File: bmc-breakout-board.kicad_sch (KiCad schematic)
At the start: 7 parts

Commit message: [#92504] Prepare schematic for new peripherals
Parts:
- removed TP1, TP2: 5001, bmc-breakout-board-footprints:Test_Point_D1.02mm, symbol bmc-breakout-board:5001
- N1: footprint bmc-breakout-board-footprints:antmicro-logo_scaled_20mm_mask -> antmicro-footprints:antmicro-logo_scaled_20mm_mask
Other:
- removed sheet Edge Connectors
- added sheet DC-SCM 2.1 connector (dc-scm-connector.kicad_sch)
- moved on the sheet: N1, N2

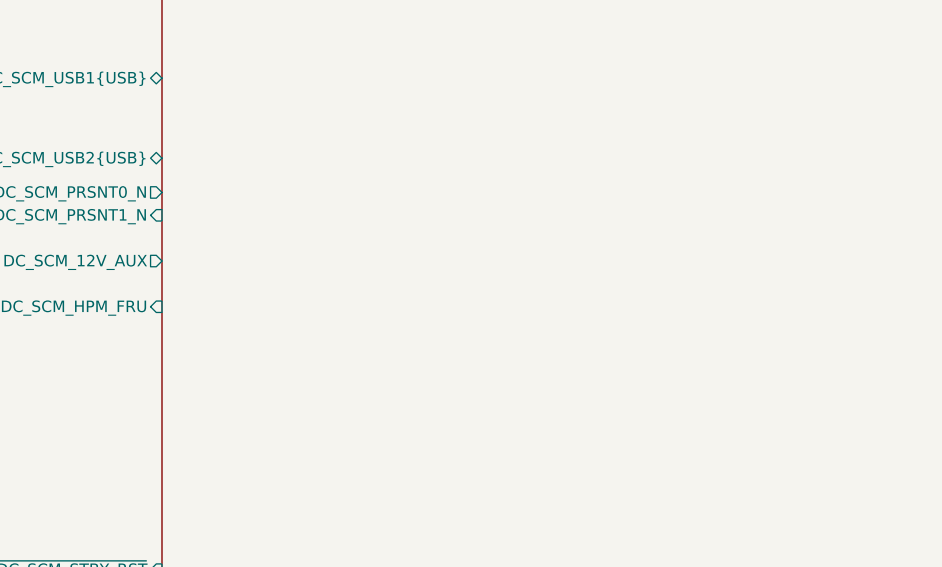
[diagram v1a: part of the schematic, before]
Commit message: [#92504] Create power schematic, change 12V connector
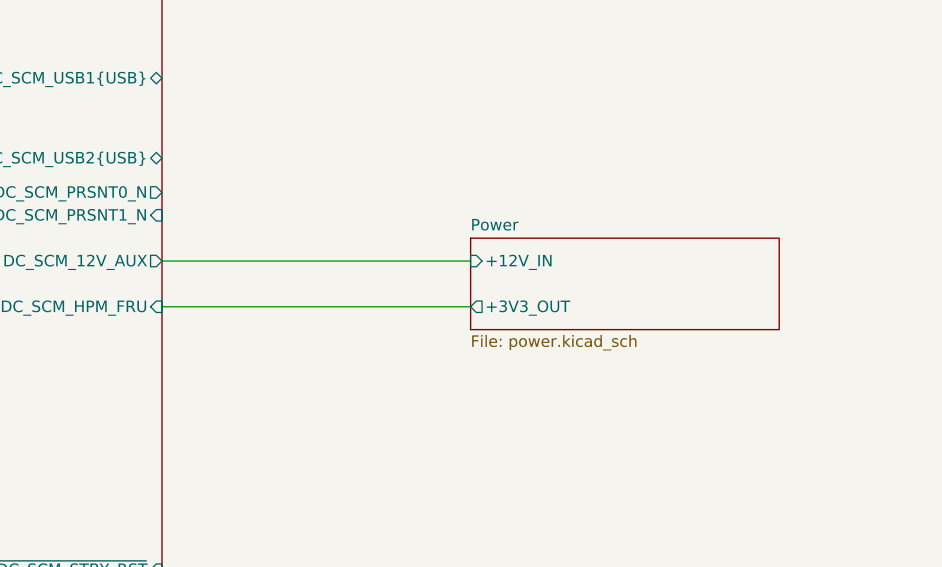
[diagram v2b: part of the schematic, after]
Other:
- added sheet Power (power.kicad_sch)
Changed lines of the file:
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@@
+		)
+	)
+	(wire
+		(pts
+			(xy 57.15 59.69) (xy 91.44 59.69)
+		)
+		(stroke
+			(width 0)
+			(type default)
+		)
+	)
+	(wire
+		(pts
+			(xy 57.15 64.77) (xy 91.44 64.77)
+		)
+		(stroke
+			(width 0)
+			(type default)
 		)
 	)
@@
 				)
 			)
+		)
+	)
+	(sheet
+		(at 91.44 57.15)
+		(size 34.29 10.16)
+		(exclude_from_sim no)
+		(in_bom yes)
+		(on_board yes)
+		(dnp no)
+		(fields_autoplaced yes)
+		(stroke
+			(width 0.1524)
+			(type solid)
+		)
+		(fill
+			(color 0 0 0 0.0000)
+		)
+		(property "Sheetname" "Power"
+			(at 91.44 56.4384 0)
+			(effects
+				(font
+					(size 1.27 1.27)
+				)
+				(justify left bottom)
+			)
+		)
+		(property "Sheetfile" "power.kicad_sch"
+			(at 91.44 67.8946 0)
+			(effects
+				(font
+					(size 1.27 1.27)
+				)
+				(justify left top)
+			)
+		)
+		(pin "+12V_IN" input
+			(at 91.44 59.69 180)
+			(effects
+				(font
+					(size 1.27 1.27)
+				)
+				(justify left)
+			)
+		)
+		(pin "+3V3_OUT" output
+			(at 91.44 64.77 180)
+			(effects
+				(font
+					(size 1.27 1.27)
+				)
+				(justify left)
+			)
+		)
+		(instances
+			(project "bmc-breakout-board"
+				(path "/5d67ef28-5805-4f87-b722-2926dabf7f6e"
+					(page "3")
+				)
+			)

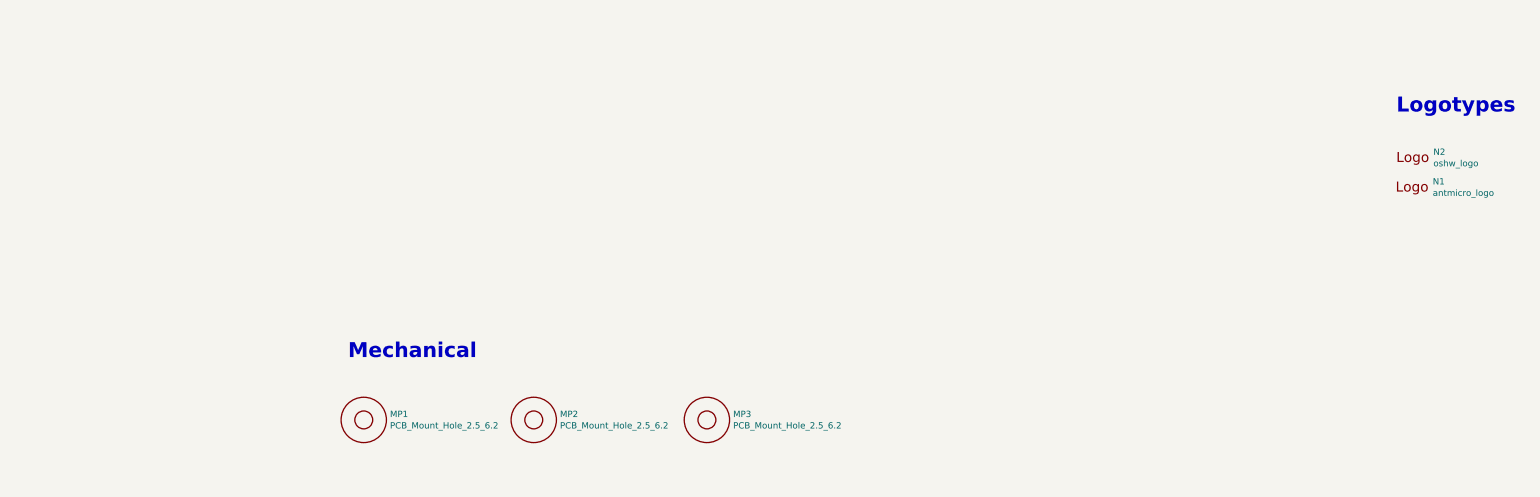
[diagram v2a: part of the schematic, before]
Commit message: [#92504] Remove micro USB and USB A
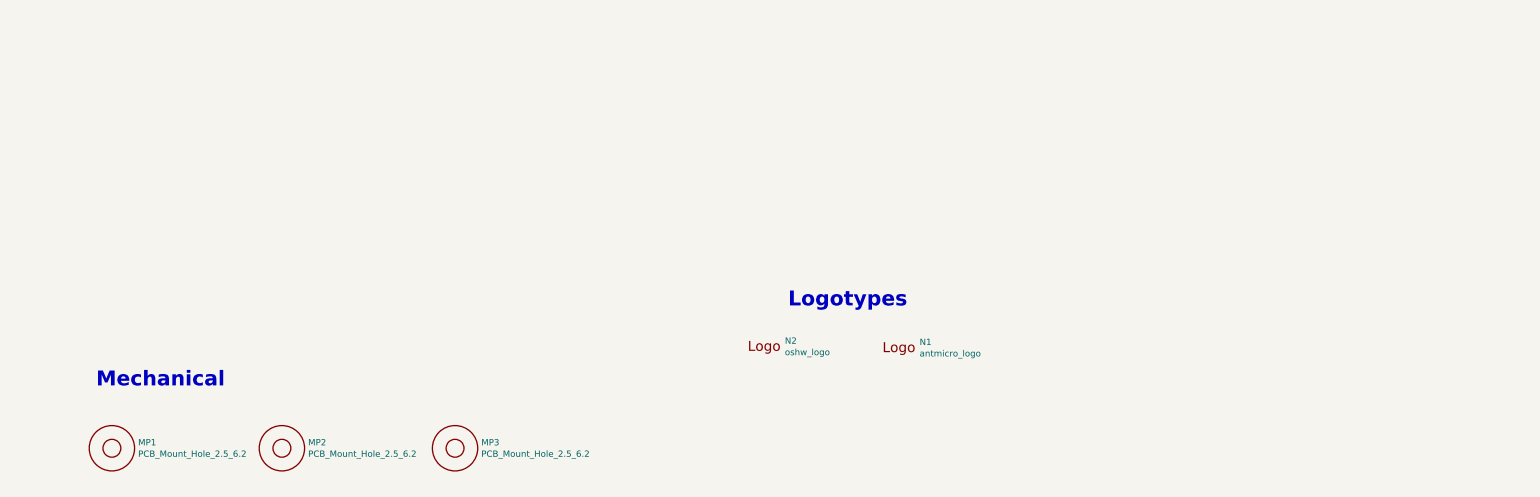
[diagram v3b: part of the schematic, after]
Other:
- moved on the sheet: MP1, MP2, MP3, N1, N2
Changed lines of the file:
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@@
 	(text "Logotypes"
 		(exclude_from_sim no)
-		(at 378.46 208.28 0)
+		(at 255.778 247.396 0)
 		(effects
 			(font
@@
 	(text "Mechanical"
 		(exclude_from_sim no)
-		(at 167.005 257.81 0)
+		(at 116.205 263.525 0)
 		(effects
 			(font
@@
 	)
 	(image
-		(at 392.43 240.03)
+		(at 288.925 272.415)
 		(scale 0.15)
 		(data "iVBORw0KGgoAAAANSUhEUgAABLAAAASwCAIAAABkQySYAAAAA3NCSVQICAjb4U/gAAAACXBIWXMA"
@@
 	)
 	(image
-		(at 354.33 239.8522)
+		(at 250.825 272.2372)
 		(scale 0.4)
 		(data "iVBORw0KGgoAAAANSUhEUgAABPcAAAGUCAYAAABZQseRAAAABHNCSVQICAgIfAhkiAAAAAlwSFlz"
@@
 	(symbol
 		(lib_id "bmc-breakout-board:antmicro_logo")
-		(at 380.365 224.155 0)
+		(at 276.86 256.54 0)
 		(unit 1)
 		(exclude_from_sim no)
@@
 		(dnp no)
 		(property "Reference" "N1"
-			(at 385.8006 221.7928 0)
+			(at 282.2956 254.1778 0)
 			(effects
 				(font
@@
 		)
 		(property "Value" "antmicro_logo"
-			(at 385.8006 224.1042 0)
+			(at 282.2956 256.4892 0)
 			(effects
 				(font
@@
 		)
 		(property "Footprint" "antmicro-footprints:antmicro-logo_scaled_20mm_mask"
-			(at 377.825 217.805 0)
+			(at 274.32 250.19 0)
 			(effects
 				(font
@@
 		)
 		(property "Datasheet" ""
-			(at 380.365 215.265 0)
+			(at 276.86 247.65 0)
 			(effects
 				(font
@@
 		)
 		(property "Description" ""
-			(at 380.365 224.155 0)
+			(at 276.86 256.54 0)
 			(effects
 				(font
@@
 	(symbol
 		(lib_id "bmc-breakout-board:oshw_logo")
-		(at 381 215.9 0)
+		(at 250.19 254 0)
 		(unit 1)
 		(exclude_from_sim no)
@@
 		(dnp no)
 		(property "Reference" "N2"
-			(at 385.9276 215.8238 0)
+			(at 255.1176 253.9238 0)
 			(effects
 				(font
@@
 		)
 		(property "Value" "oshw_logo"
-			(at 385.9276 218.1352 0)
+			(at 255.1176 256.2352 0)
 			(effects
 				(font
@@
 		)
 		(property "Footprint" "bmc-breakout-board-footprints:oshw-logo"
-			(at 381.508 221.996 0)
+			(at 250.698 260.096 0)
 			(effects
 				(font
@@
 		)
 		(property "Datasheet" ""
-			(at 381 215.9 0)
+			(at 250.19 254 0)
 			(effects
 				(font
@@
 		)
 		(property "Description" ""
-			(at 381 215.9 0)
+			(at 250.19 254 0)
 			(effects
 				(font
@@
 	(symbol
 		(lib_id "bmc-breakout-board:PCB_Mount_Hole_2.5_6.2")
-		(at 204.47 269.875 0)
+		(at 153.67 275.59 0)
 		(unit 1)
 		(exclude_from_sim no)
@@
 		(dnp no)
 		(property "Reference" "MP2"
-			(at 209.7532 268.7066 0)
+			(at 158.9532 274.4216 0)
 			(effects
 				(font
@@
 		)
 		(property "Value" "PCB_Mount_Hole_2.5_6.2"
-			(at 209.7532 271.018 0)
+			(at 158.9532 276.733 0)
 			(effects
 				(font
@@
 		)
 		(property "Footprint" "bmc-breakout-board-footprints:Mount-hole-M2.5"
-			(at 224.79 252.095 0)
+			(at 173.99 257.81 0)
 			(effects
 				(font
@@
 		)
 		(property "Datasheet" ""
-			(at 228.6 249.555 0)
+			(at 177.8 255.27 0)
 			(effects
 				(font
@@
 		)
 		(property "Description" ""
-			(at 204.47 269.875 0)
+			(at 153.67 275.59 0)
 			(effects
 				(font
@@
 	(symbol
 		(lib_id "bmc-breakout-board:PCB_Mount_Hole_2.5_6.2")
-		(at 239.395 269.875 0)
+		(at 188.595 275.59 0)
 		(unit 1)
 		(exclude_from_sim no)
@@
 		(dnp no)
 		(property "Reference" "MP3"
-			(at 244.6782 268.7066 0)
+			(at 193.8782 274.4216 0)
 			(effects
 				(font
@@
 		)
 		(property "Value" "PCB_Mount_Hole_2.5_6.2"
-			(at 244.6782 271.018 0)
+			(at 193.8782 276.733 0)
 			(effects
 				(font
@@
 		)
 		(property "Footprint" "bmc-breakout-board-footprints:Mount-hole-M2.5"
-			(at 259.715 252.095 0)
+			(at 208.915 257.81 0)
 			(effects
 				(font
@@
 		)
 		(property "Datasheet" ""
-			(at 263.525 249.555 0)
+			(at 212.725 255.27 0)
 			(effects
 				(font
@@
 		)
 		(property "Description" ""
-			(at 239.395 269.875 0)
+			(at 188.595 275.59 0)
 			(effects
 				(font
@@
 	(symbol
 		(lib_id "bmc-breakout-board:PCB_Mount_Hole_2.5_6.2")
-		(at 170.18 269.875 0)
+		(at 119.38 275.59 0)
 		(unit 1)
 		(exclude_from_sim no)
@@
 		(dnp no)
 		(property "Reference" "MP1"
-			(at 175.4632 268.7066 0)
+			(at 124.6632 274.4216 0)
 			(effects
 				(font
@@
 		)
 		(property "Value" "PCB_Mount_Hole_2.5_6.2"
-			(at 175.4632 271.018 0)
+			(at 124.6632 276.733 0)
 			(effects
 				(font
@@
 		)
 		(property "Footprint" "bmc-breakout-board-footprints:Mount-hole-M2.5"
-			(at 190.5 252.095 0)
+			(at 139.7 257.81 0)
 			(effects
 				(font
@@
 		)
 		(property "Datasheet" ""
-			(at 194.31 249.555 0)
+			(at 143.51 255.27 0)
 			(effects
 				(font
@@
 		)
 		(property "Description" ""
-			(at 170.18 269.875 0)
+			(at 119.38 275.59 0)
 			(effects
 				(font

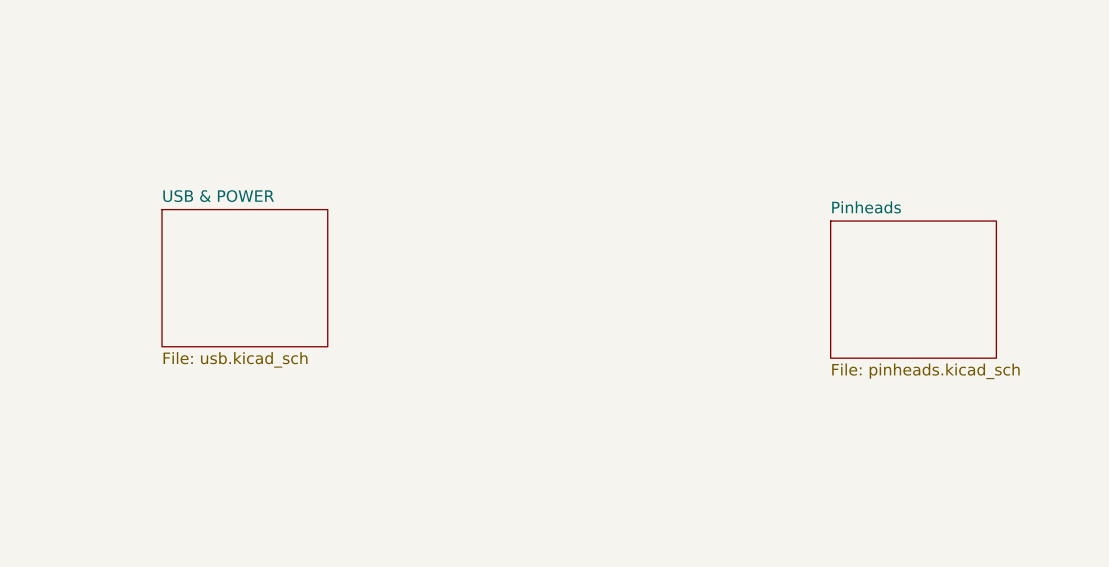
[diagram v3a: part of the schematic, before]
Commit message: [#92504] Remove old pinheads
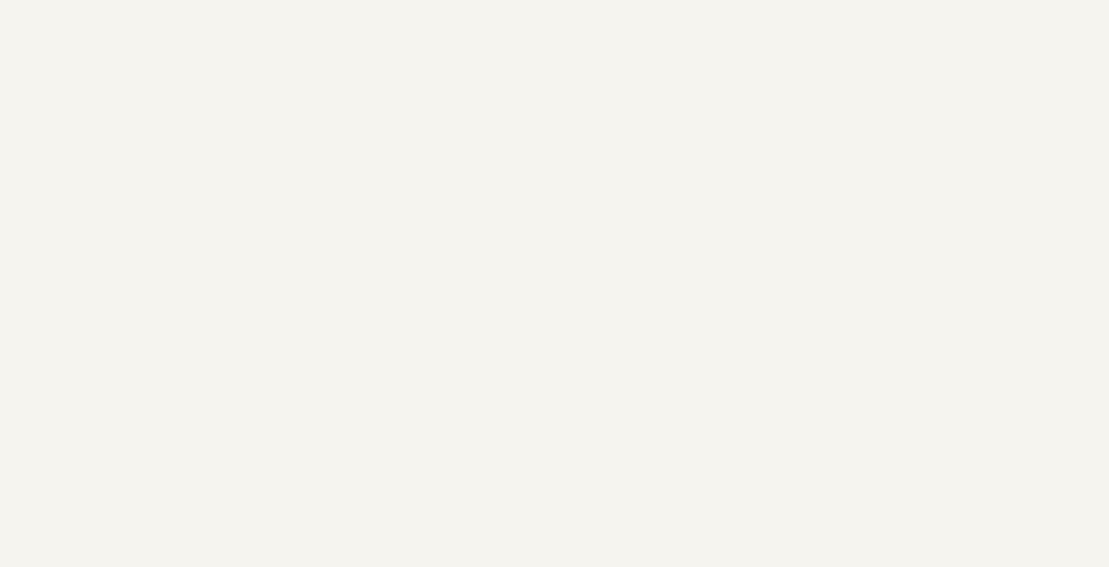
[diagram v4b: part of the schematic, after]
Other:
- removed sheet Pinheads
- removed sheet USB & POWER
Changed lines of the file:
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@@
-	)
-	(sheet
-		(at 351.155 101.6)
-		(size 18.415 15.24)
-		(exclude_from_sim no)
-		(in_bom yes)
-		(on_board yes)
-		(dnp no)
-		(fields_autoplaced yes)
-		(stroke
-			(width 0)
-			(type solid)
-		)
-		(fill
-			(color 0 0 0 0.0000)
-		)
-		(property "Sheetname" "Pinheads"
-			(at 351.155 100.8884 0)
-			(effects
-				(font
-					(size 1.27 1.27)
-				)
-				(justify left bottom)
-			)
-		)
-		(property "Sheetfile" "pinheads.kicad_sch"
-			(at 351.155 117.4246 0)
-			(effects
-				(font
-					(size 1.27 1.27)
-				)
-				(justify left top)
-			)
-		)
-		(instances
-			(project "bmc-breakout-board"
-				(path "/5d67ef28-5805-4f87-b722-2926dabf7f6e"
-					(page "2")
-				)
-			)
-		)
-	)
-	(sheet
-		(at 276.86 100.33)
-		(size 18.415 15.24)
-		(exclude_from_sim no)
-		(in_bom yes)
-		(on_board yes)
-		(dnp no)
-		(fields_autoplaced yes)
-		(stroke
-			(width 0)
-			(type solid)
-		)
-		(fill
-			(color 0 0 0 0.0000)
-		)
-		(property "Sheetname" "USB & POWER"
-			(at 276.86 99.6184 0)
-			(effects
-				(font
-					(size 1.27 1.27)
-				)
-				(justify left bottom)
-			)
-		)
-		(property "Sheetfile" "usb.kicad_sch"
-			(at 276.86 116.1546 0)
-			(effects
-				(font
-					(size 1.27 1.27)
-				)
-				(justify left top)
-			)
-		)
-		(instances
-			(project "bmc-breakout-board"
-				(path "/5d67ef28-5805-4f87-b722-2926dabf7f6e"
-					(page "4")
-				)
-			)
-		)
 	)
 	(sheet
